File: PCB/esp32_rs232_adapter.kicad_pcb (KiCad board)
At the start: 2 copper layers, 43 parts, among them J1 Conn_01x04_Male, J2 DB9, J3 DB9X, J4 USB_B_Micro, SW1 Flash, U1 ESP32-WROOM-32D, U2 MAX3232, U3 TP4056, U4 TPS73733

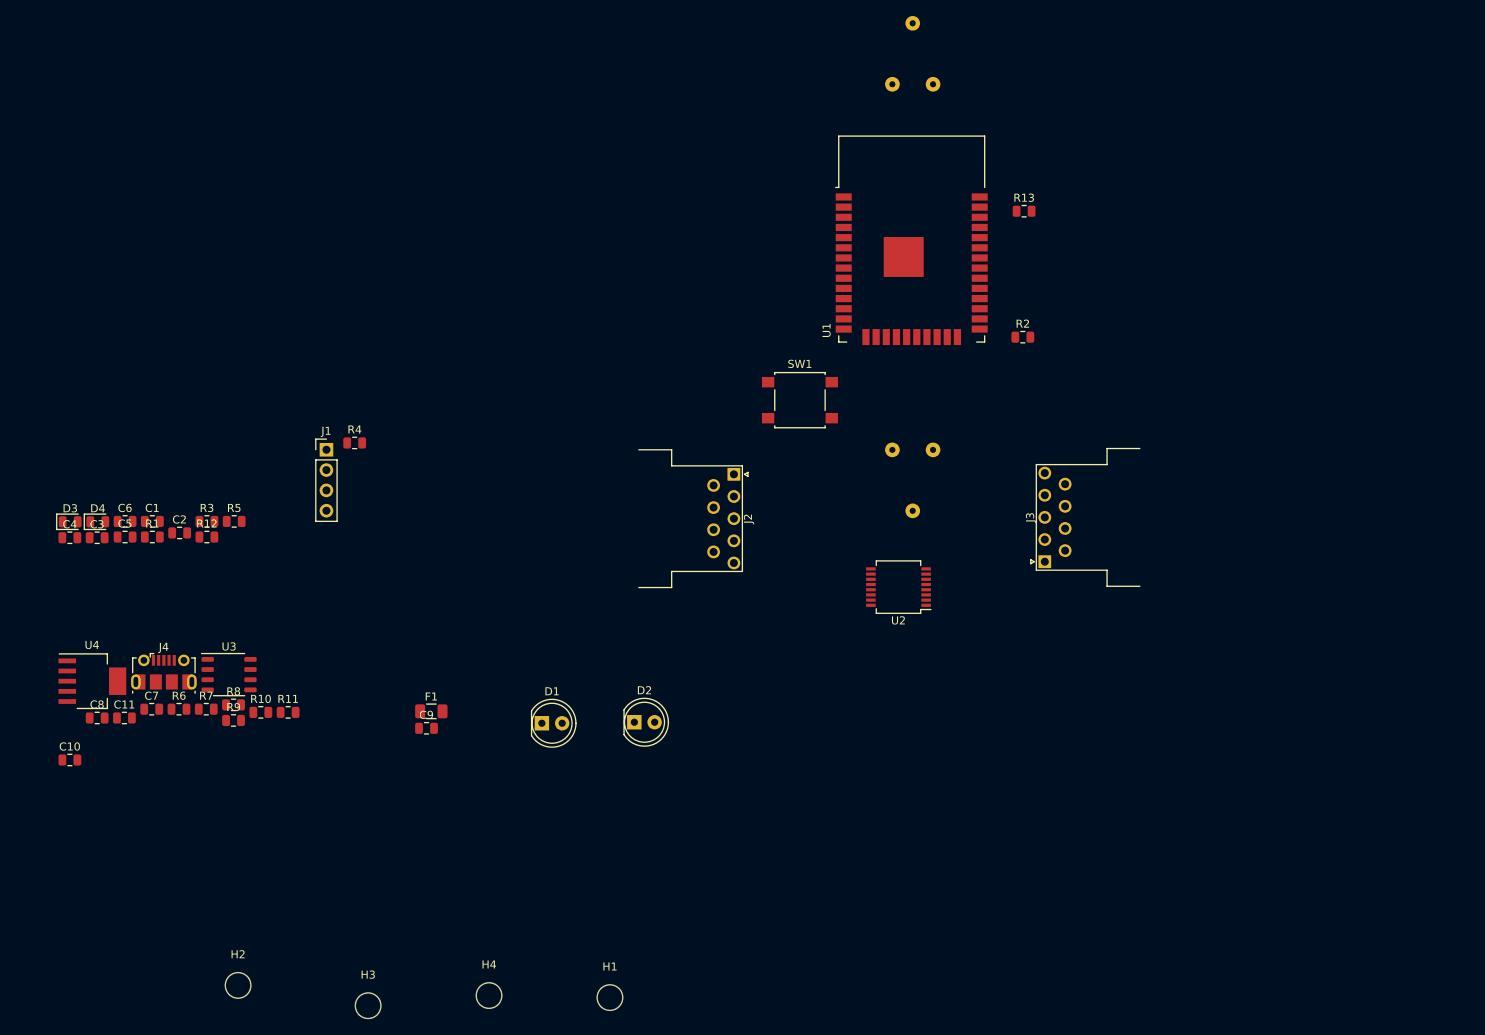
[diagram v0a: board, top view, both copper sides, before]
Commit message: change footprints. Add dip switch for null modem
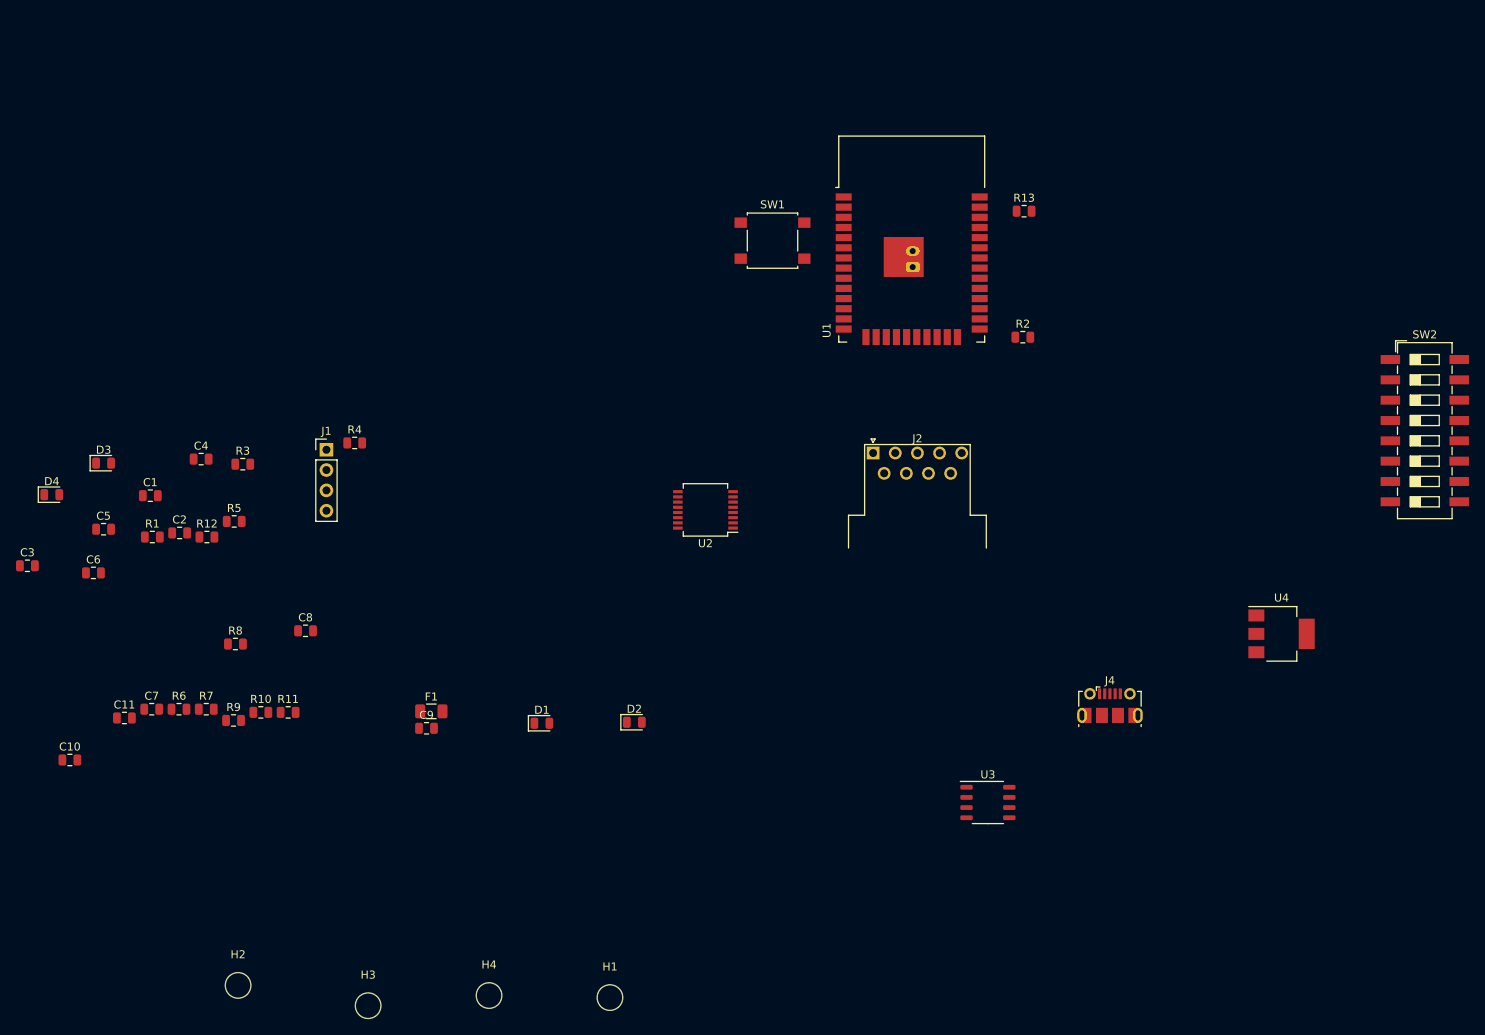
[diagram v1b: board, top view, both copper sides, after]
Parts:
- removed J3: DB9X, Connector_Dsub:DSUB-9_Male_Horizontal_P2.77x2.54mm_EdgePinOffset9.40mm
- added SW2: Null_Modem_Selector, Button_Switch_SMD:SW_DIP_SPSTx08_Slide_6.7x21.88mm_W8.61mm_P2.54mm_LowProfile, F.Cu at (219.7, 114.8)
- BT1: footprint power_supplies:Keystone_18650_Battery_Clip -> Connector_JST:JST_PH_B2B-PH-K_1x02_P2.00mm_Vertical
- D1, D2: footprint LED_THT:LED_D5.0mm -> LED_SMD:LED_0805_2012Metric
- U4: value TPS73733 -> AMS1117; footprint Package_TO_SOT_SMD:SOT-223-6_TabPin3 -> Package_TO_SOT_SMD:SOT-223-3_TabPin2
- moved U4 148.8 mm to (201.8, 140.2)
- moved J4 118.3 mm to (180.4, 149.2)
- moved U3 96.2 mm to (165.1, 161.3)
- moved C8 28.2 mm to (79.8, 139.8)
- moved U2 26.0 mm to (129.8, 124.7)
- moved SW1 20.2 mm to (138.2, 91.1)
- moved C4 19.1 mm to (66.8, 118.4)
- moved J2 17.6 mm to (150.7, 117.6), turned to 0 degrees
- moved C3 9.40 mm to (45.0, 131.7)
- moved R3 8.45 mm to (72.0, 119.0)
- moved D3 8.43 mm to (54.6, 118.9)
- moved R8 7.61 mm to (71.0, 141.5)
- moved C6 7.55 mm to (53.3, 132.6)
- moved D4 6.68 mm to (48.1, 122.8)
- moved C1 3.23 mm to (60.4, 122.9)
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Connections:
- C10 pad 1: Net-(C10-Pad1) -> +3V3
- J2 pad 2: /TXD_RS232 -> Net-(J2-Pad2)
- J2 pad 3: /RXD_RS232 -> Net-(J2-Pad3)
- J2 pad 7: /CTS_RS232 -> Net-(J2-Pad7)
- J2 pad 8: /RTS_RS232 -> Net-(J2-Pad8)
- U4 pad 1: +BATT -> GND
- U4 pad 3: GND -> +BATT

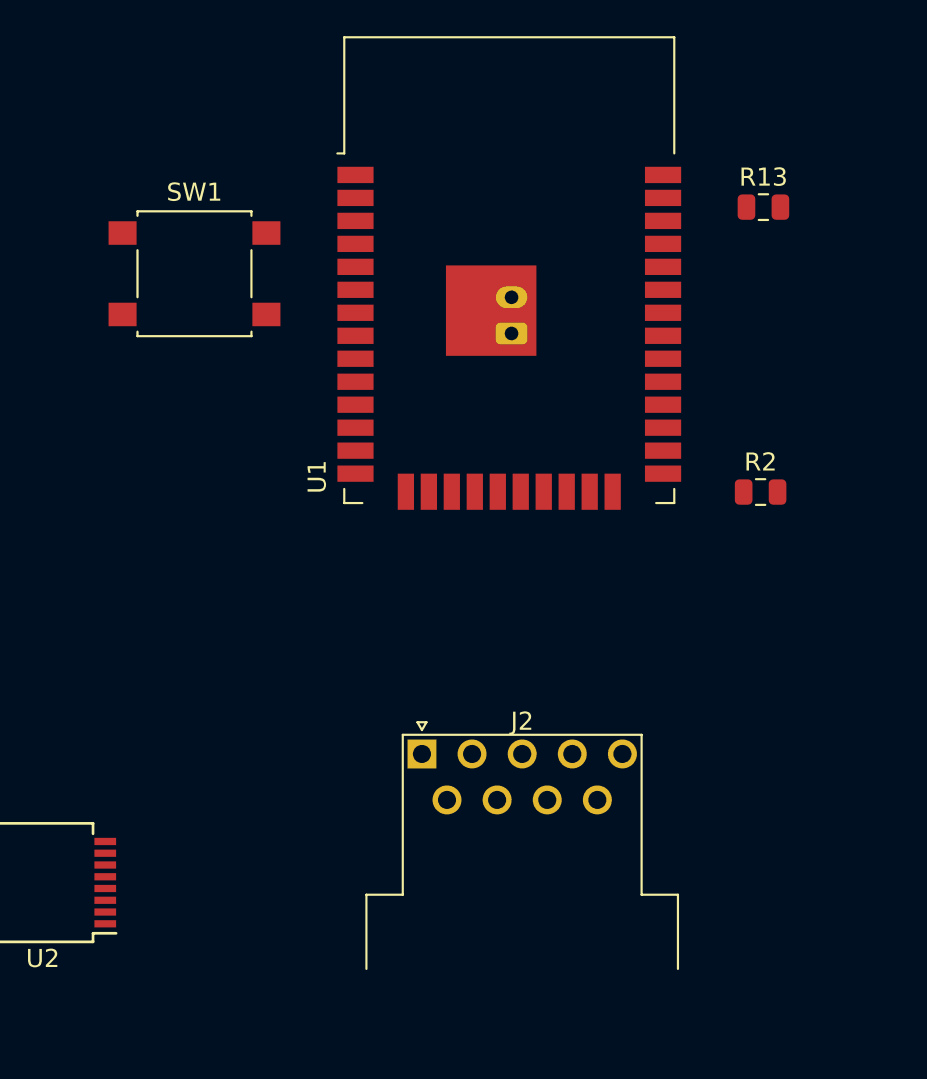
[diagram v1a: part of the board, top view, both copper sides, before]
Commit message: More footprint swaps
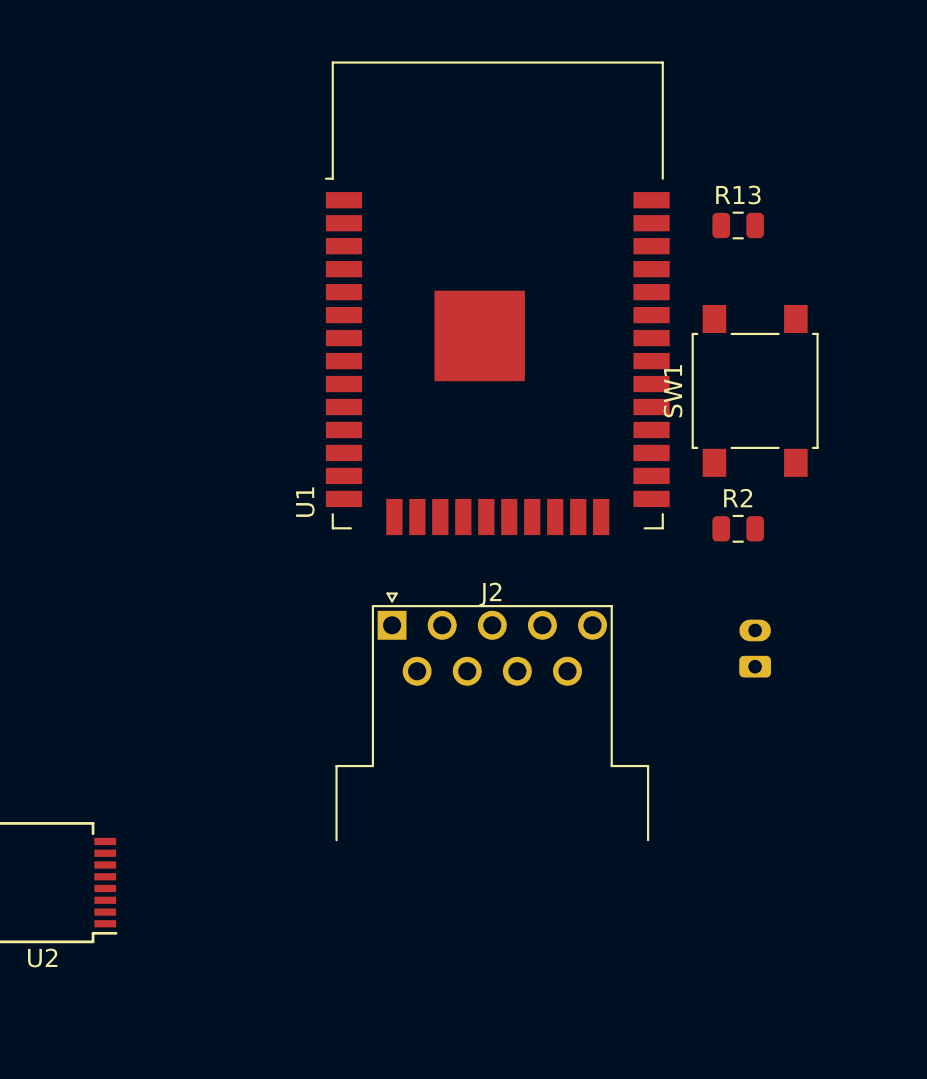
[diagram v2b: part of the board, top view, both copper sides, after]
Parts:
- moved SW1 31.7 mm to (169.2, 97.5), turned to 90 degrees
- moved BT1 22.8 mm to (169.2, 112.8)
- moved J2 7.30 mm to (149.1, 110.5)
- moved R2 2.38 mm to (168.2, 105.2)
- moved R13 1.73 mm to (168.2, 88.4)
- moved U1 1.53 mm to (154.9, 95.2)
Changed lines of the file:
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@@
-(kicad_pcb (version 20171130) (host pcbnew 5.0.2-bee76a0~70~ubuntu18.04.1)
+(kicad_pcb (version 20171130) (host pcbnew "(5.0.2)-1")
   (general
     (thickness 1.6)
@@
     (solder_mask_min_width 0.25)
     (aux_axis_origin 0 0)
-    (visible_elements FFFFFF7F)
+    (visible_elements 7FFFFFFF)
     (pcbplotparams
       (layerselection 0x010fc_ffffffff)
@@
   )
   (module Connector_Dsub:DSUB-9_Male_Horizontal_P2.77x2.54mm_EdgePinOffset9.40mm (layer F.Cu)
-    (at 150.749 117.602)
+    (at 149.098 110.49)
     (descr "9-pin D-Sub connector, horizontal/angled (90 deg), THT-mount, male, pitch 2.77x2.54mm, pin-PCB-offset 9.4mm, see http://docs-europe.electrocomponents.com/webdocs/1585/0900766b81585df2.pdf")
     (tags "9-pin D-Sub connector horizontal angled 90deg THT male pitch 2.77x2.54mm pin-PCB-offset 9.4mm")
@@
   )
   (module Resistor_SMD:R_0805_2012Metric (layer F.Cu)
-    (at 169.4665 103.124)
+    (at 168.2265 105.156)
     (descr "Resistor SMD 0805 (2012 Metric), square (rectangular) end terminal, IPC_7351 nominal, (Body size source: https://docs.google.com/spreadsheets/d/1BsfQQcO9C6DZCsRaXUlFlo91Tg2WpOkGARC1WS5S8t0/edit?usp=sharing), generated with kicad-footprint-generator")
     (tags resistor)
@@
   )
   (module Resistor_SMD:R_0805_2012Metric (layer F.Cu)
-    (at 169.6235 87.376)
+    (at 168.2265 88.392)
     (descr "Resistor SMD 0805 (2012 Metric), square (rectangular) end terminal, IPC_7351 nominal, (Body size source: https://docs.google.com/spreadsheets/d/1BsfQQcO9C6DZCsRaXUlFlo91Tg2WpOkGARC1WS5S8t0/edit?usp=sharing), generated with kicad-footprint-generator")
     (tags resistor)
@@
   )
   (module Button_Switch_SMD:SW_SPST_B3S-1000 (layer F.Cu)
-    (at 138.176 91.059)
+    (at 169.164 97.536 90)
     (descr "Surface Mount Tactile Switch for High-Density Packaging")
     (tags "Tactile Switch")
     (attr smd)
-    (fp_text reference SW1 (at 0 -4.5) (layer F.SilkS)
-      (effects (font (size 1 1) (thickness 0.15)))
-    )
-    (fp_text value Flash (at 0 4.5) (layer F.Fab)
-      (effects (font (size 1 1) (thickness 0.15)))
-    )
-    (fp_text user %R (at 0 -4.5) (layer F.Fab)
+    (fp_text reference SW1 (at 0 -4.5 90) (layer F.SilkS)
+      (effects (font (size 1 1) (thickness 0.15)))
+    )
+    (fp_text value Flash (at 0 4.5 90) (layer F.Fab)
+      (effects (font (size 1 1) (thickness 0.15)))
+    )
+    (fp_text user %R (at 0 -4.5 90) (layer F.Fab)
       (effects (font (size 1 1) (thickness 0.15)))
     )
@@
     (fp_line (start 3 3.3) (end -3 3.3) (layer F.Fab) (width 0.1))
     (fp_line (start -3 3.3) (end -3 -3.3) (layer F.Fab) (width 0.1))
-    (pad 1 smd rect (at -3.975 -2.25) (size 1.55 1.3) (layers F.Cu F.Paste F.Mask)
+    (pad 1 smd rect (at -3.975 -2.25 90) (size 1.55 1.3) (layers F.Cu F.Paste F.Mask)
       (net 28 "Net-(R3-Pad2)"))
-    (pad 1 smd rect (at 3.975 -2.25) (size 1.55 1.3) (layers F.Cu F.Paste F.Mask)
+    (pad 1 smd rect (at 3.975 -2.25 90) (size 1.55 1.3) (layers F.Cu F.Paste F.Mask)
       (net 28 "Net-(R3-Pad2)"))
-    (pad 2 smd rect (at -3.975 2.25) (size 1.55 1.3) (layers F.Cu F.Paste F.Mask)
-      (net 1 GND))
-    (pad 2 smd rect (at 3.975 2.25) (size 1.55 1.3) (layers F.Cu F.Paste F.Mask)
+    (pad 2 smd rect (at -3.975 2.25 90) (size 1.55 1.3) (layers F.Cu F.Paste F.Mask)
+      (net 1 GND))
+    (pad 2 smd rect (at 3.975 2.25 90) (size 1.55 1.3) (layers F.Cu F.Paste F.Mask)
       (net 1 GND))
     (model ${KISYS3DMOD}/Button_Switch_SMD.3dshapes/SW_SPST_B3S-1000.wrl
@@
   )
   (module RF_Module:ESP32-WROOM-32 (layer F.Cu)
-    (at 155.575 93.853)
+    (at 154.94 95.25)
     (descr "Single 2.4 GHz Wi-Fi and Bluetooth combo chip https://www.espressif.com/sites/default/files/documentation/esp32-wroom-32_datasheet_en.pdf")
     (tags "Single 2.4 GHz Wi-Fi and Bluetooth combo  chip")
@@
   )
   (module Connector_JST:JST_PH_B2B-PH-K_1x02_P2.00mm_Vertical (layer B.Cu)
-    (at 155.702 94.361 90)
+    (at 169.164 112.776 90)
     (descr "JST PH series connector, B2B-PH-K (http://www.jst-mfg.com/product/pdf/eng/ePH.pdf), generated with kicad-footprint-generator")
     (tags "connector JST PH side entry")

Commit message: PCB finished
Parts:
- added Q1: IRF7404, Package_SO:SOIC-8_3.9x4.9mm_P1.27mm, B.Cu at (169.7, 116.2)
- added R14: 10k, Resistor_SMD:R_0805_2012Metric, B.Cu at (163.7, 114.7)
- added SW3: SW_SPST, Button_Switch_THT:SW_CuK_JS202011CQN_DPDT_Straight, F.Cu at (167.1, 103.3)
- C1, C10, C11, C2, C3, C4, C5, C6, C9, R1, R2, R3, R4, R5, U2, U4: moved to B.Cu
- J2: footprint Connector_Dsub:DSUB-9_Male_Horizontal_P2.77x2.54mm_EdgePinOffset9.40mm -> Connector_Dsub:DSUB-9_Male_Horizontal_P2.77x2.84mm_EdgePinOffset4.94mm_Housed_MountingHolesOffset7.48mm
- moved D4 123.0 mm to (167.0, 91.5), turned to 90 degrees
- moved C10 115.4 mm to (149.1, 96.2), turned to 90 degrees
- moved C3 112.2 mm to (156.8, 122.4), turned to 180 degrees
- moved H1 111.9 mm to (174.9, 89.4)
- moved R7 111.6 mm to (175.0, 120.2), turned to 90 degrees
- moved C7 111.4 mm to (169.0, 124.2), turned to 270 degrees
- moved R6 110.2 mm to (171.2, 124.2), turned to 270 degrees
- moved C11 108.6 mm to (151.1, 96.2), turned to 90 degrees
- moved R8 108.2 mm to (177.2, 120.2), turned to 90 degrees
- moved H3 103.4 mm to (174.9, 131.2)
- moved H4 101.4 mm to (135.2, 89.4)
- moved R9 100.6 mm to (166.9, 121.1), turned to 270 degrees
- moved R10 100.1 mm to (166.9, 112.2), turned to 90 degrees
- moved R11 98.4 mm to (166.9, 108.7), turned to 90 degrees
- moved C6 96.5 mm to (147.9, 113.6), turned to 270 degrees
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- renumbered SW1 to Flash
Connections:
- net Net-(BT1-Pad1) renamed /power_supply/P_Batt_0
- net Net-(C7-Pad1) renamed /power_supply/P5_1
- net Net-(J4-Pad1) renamed /power_supply/P5_0
- C9 pad 1: +BATT -> /power_supply/P_Batt_1
- R10 pad 1: +BATT -> /power_supply/P_Batt_1
- U4 pad 3: +BATT -> /power_supply/P_Batt_1
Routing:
- net /power_supply/Vbatt_sig: track 0.00 -> 56.8 mm, vias 0 -> 2
- net /power_supply/P_Batt_1: track 0.00 -> 50.4 mm, vias 0 -> 2
- net /TXD: track 0.00 -> 37.1 mm, vias 0 -> 1
- net /RXD: track 0.00 -> 35.7 mm, vias 0 -> 3
- net +3V3: track 0.00 -> 35.6 mm, vias 0 -> 3
- net /RTS: track 0.00 -> 35.4 mm, vias 0 -> 1
- net Net-(R3-Pad2): track 0.00 -> 33.3 mm, vias 0 -> 5
- net Net-(J2-Pad7): track 0.00 -> 32.3 mm, vias 0 -> 2
- net /power_supply/P5_0: track 0.00 -> 25.2 mm, vias 0 -> 2
- net Net-(J2-Pad2): track 0.00 -> 24.6 mm, vias 0 -> 1
- net /CTS: track 0.00 -> 22.9 mm, vias 0 -> 1
- net /TXD_RS232: track 0.00 -> 22.4 mm, vias 0 -> 1
- net /RXD_RS232: track 0.00 -> 20.1 mm, vias 0 -> 1
- net Net-(J2-Pad8): track 0.00 -> 18.3 mm, vias 0 -> 2
- net GND: track 0.00 -> 17.9 mm, vias 0 -> 8
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- added copper zone on B.Cu, net +3V3
- added copper zone on F.Cu, net GND
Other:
- board outline added: 46.5 x 57.7 mm
- net class Power added: clearance 0.2, trace_width 0.4, via_dia 1.2, via_drill 0.6
- board text added: "Rx Tx 3.3V Gnd"
